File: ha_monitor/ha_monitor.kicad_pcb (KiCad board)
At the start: 2 copper layers, 9 parts, among them J1 0.91 OLED, J2 D1 Mini, J3 D1 Mini, J4 0.96 OLED, J5 DHT11

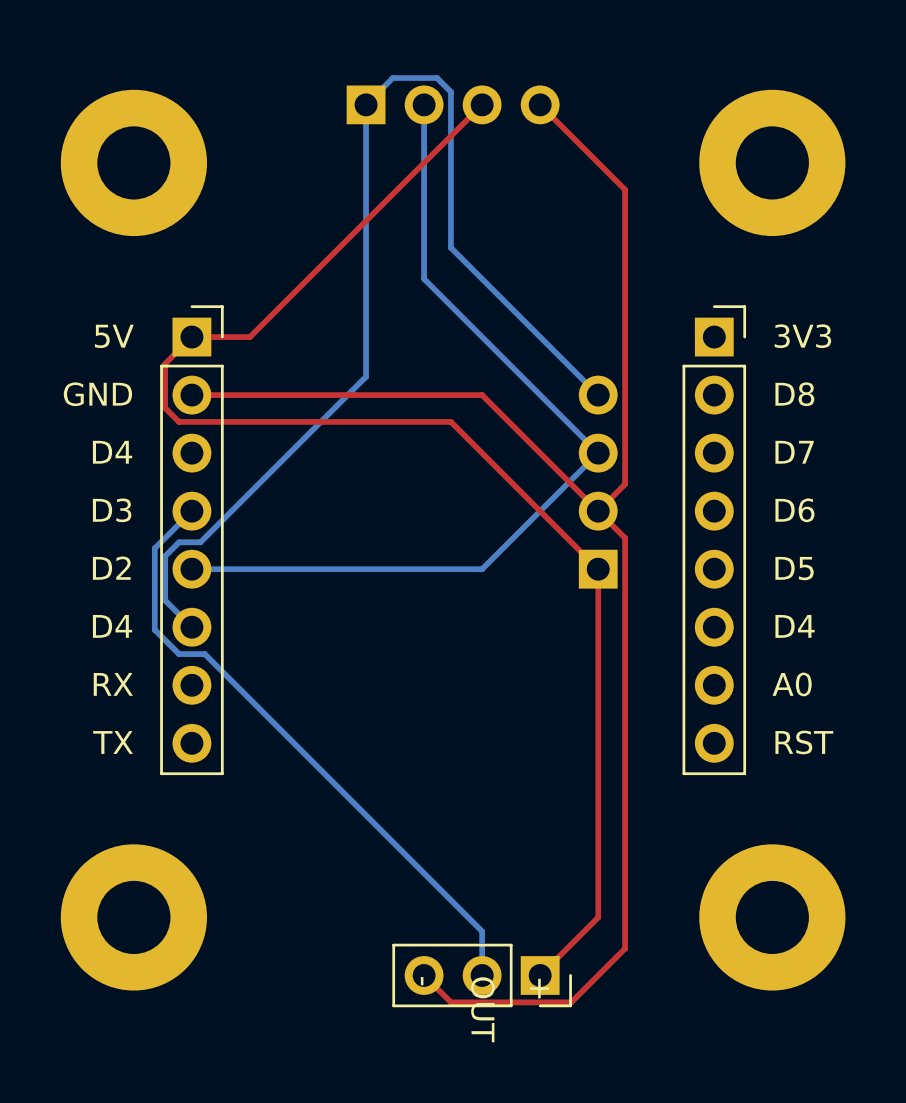
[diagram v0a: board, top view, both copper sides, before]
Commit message: Removing bad render images
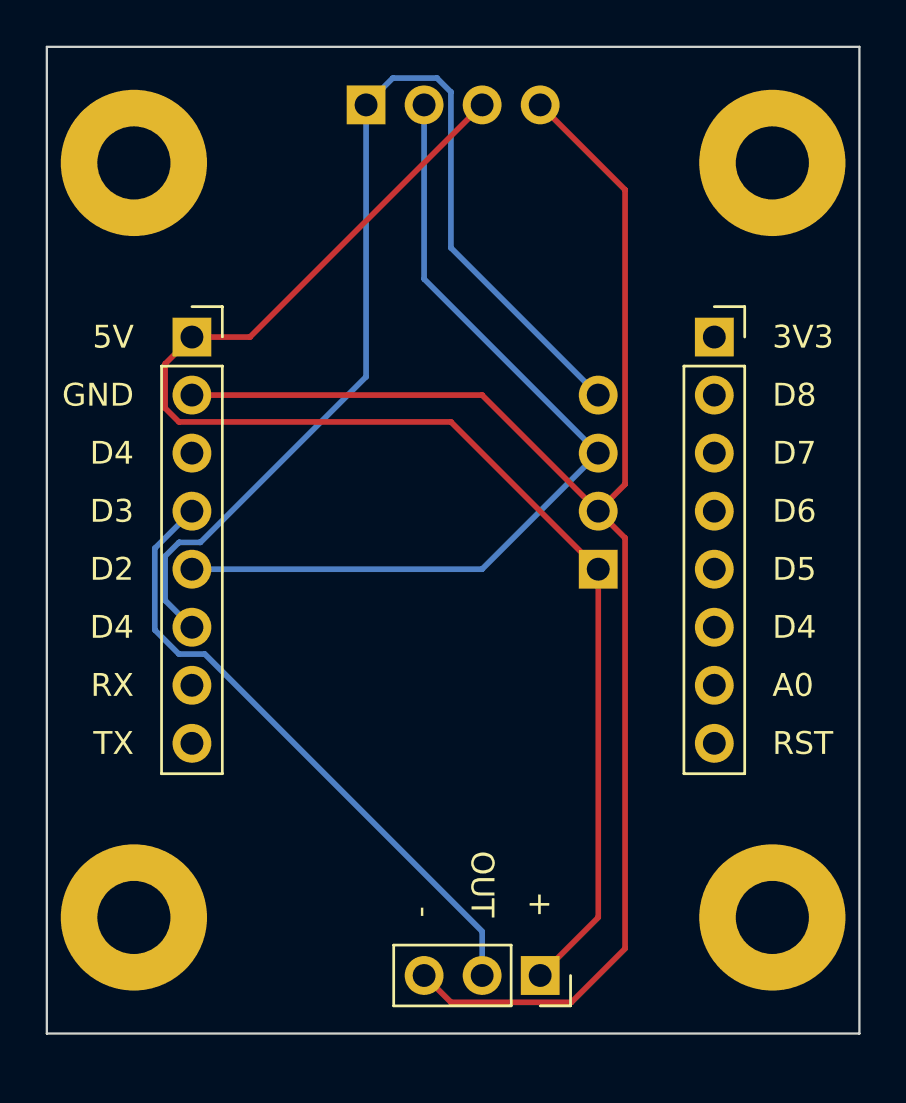
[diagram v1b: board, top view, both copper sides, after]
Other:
- board outline added: 35.6 x 43.2 mm

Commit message: Adding name silkscreen and plots
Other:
- board text added: "Home Monitor 2022 Patrick Connelly"
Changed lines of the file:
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@@
-(kicad_pcb (version 20171130) (host pcbnew 5.1.10-6.fc33)
+(kicad_pcb (version 20171130) (host pcbnew 5.1.12-1.fc33)
   (general
     (thickness 1.6)
-    (drawings 31)
+    (drawings 32)
     (tracks 40)
     (zones 0)
@@
     (visible_elements FFFFFF7F)
     (pcbplotparams
-      (layerselection 0x010fc_ffffffff)
-      (usegerberextensions false)
-      (usegerberattributes true)
-      (usegerberadvancedattributes true)
-      (creategerberjobfile true)
+      (layerselection 0x01030_ffffffff)
+      (usegerberextensions true)
+      (usegerberattributes false)
+      (usegerberadvancedattributes false)
+      (creategerberjobfile false)
       (excludeedgelayer true)
       (linewidth 0.100000)
@@
       (outputformat 1)
       (mirror false)
-      (drillshape 1)
+      (drillshape 0)
       (scaleselection 1)
-      (outputdirectory ""))
+      (outputdirectory "plots/"))
   )
   (net 0 "")
@@
     )
   )
+  (gr_text "Home Monitor\n2022 Patrick Connelly" (at 62.23 71.12) (layer B.SilkS)
+    (effects (font (size 1 1) (thickness 0.15)) (justify mirror))
+  )
   (gr_line (start 80.01 38.1) (end 80.01 81.28) (layer Edge.Cuts) (width 0.1))
